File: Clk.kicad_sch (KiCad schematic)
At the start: 12 parts, among them U5 SiT2001, U6 74LVC1G74DC, U7 74LVC1G74DC

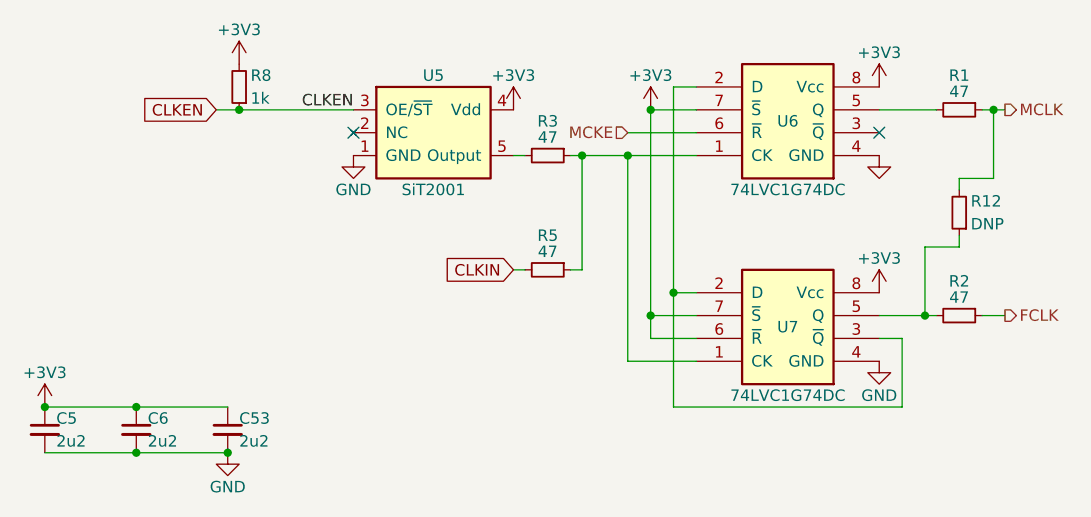
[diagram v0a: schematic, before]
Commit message: Before remove first clock input buffer
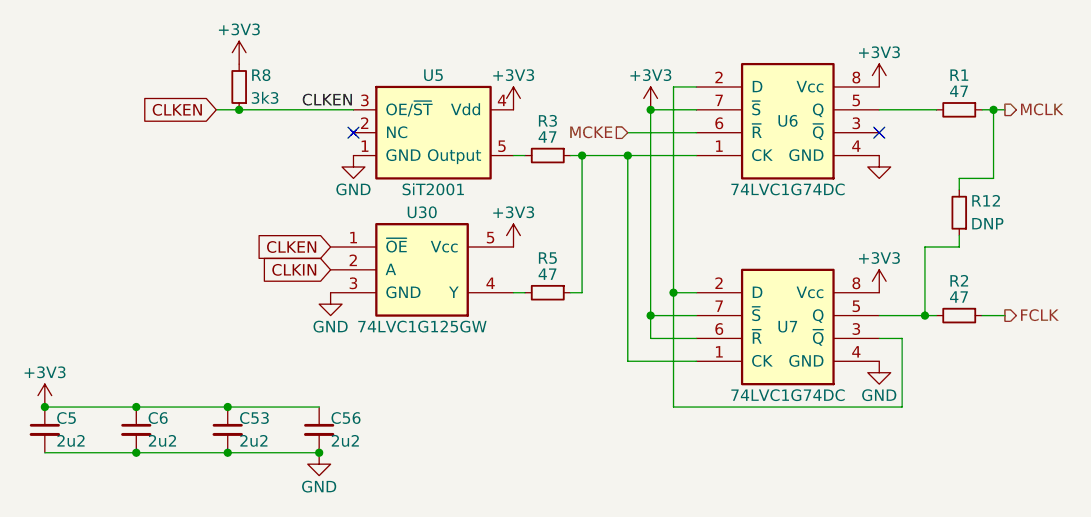
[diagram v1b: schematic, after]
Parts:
- added C56: 2u2, stdpads:C_0603, symbol Device:C_Small
- added U30: 74LVC1G125GW, stdpads:SOT-353, symbol GW_Logic:741G125GW
- R8: value 1k -> 3k3
- U5: LCSC Part (none) -> C17253174
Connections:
- net +3V3: now also C56.1, U30.5 (Vcc)
- net CLKEN: now also U30.1 (~{OE})
- net CLKIN: now also U30.2 (A); no longer R5.2
- net GND: now also C56.2, U30.3 (GND)
- new net: R5.2, U30.4 (Y)
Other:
- moved on the sheet: R5

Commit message: Final A?
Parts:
- added C55: 2u2, stdpads:C_0603, symbol Device:C_Small
- added R4: 470, stdpads:R_0603, symbol Device:R_Small
- added R9: 820, stdpads:R_0603, symbol Device:R_Small
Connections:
- net +3V3: now also R4.2
- net CLKIN: now also R4.1, R9.2
- net GND: now also C55.2, R9.1
- new net +5V: C55.1
